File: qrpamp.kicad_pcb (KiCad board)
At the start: 2 copper layers, 101 parts, among them K1 BAND3_IN, K2 BAND2_IN, K3 BAND1_IN, K4 BAND3_OUT, K5 BAND2_OUT, K6 BAND1_OUT, K7 ANT_RLY, P1 PWR, P2 PWR_SW, P3 SWD, P4 ANT, P5 RADIO, P6 PTT_IN, P7 Thumb-Joystick, Q1 MMBT6427, Q2 MMBF170, Q3 IRF510, Q4 IRF510, T1 8:8, T2 8:8, T3 2:3, T4 12:1, T5 1:12, U1 LM7805, U2 LM3940, U3 LCD-2x16, U4 STM32F401xB/C-LQFP

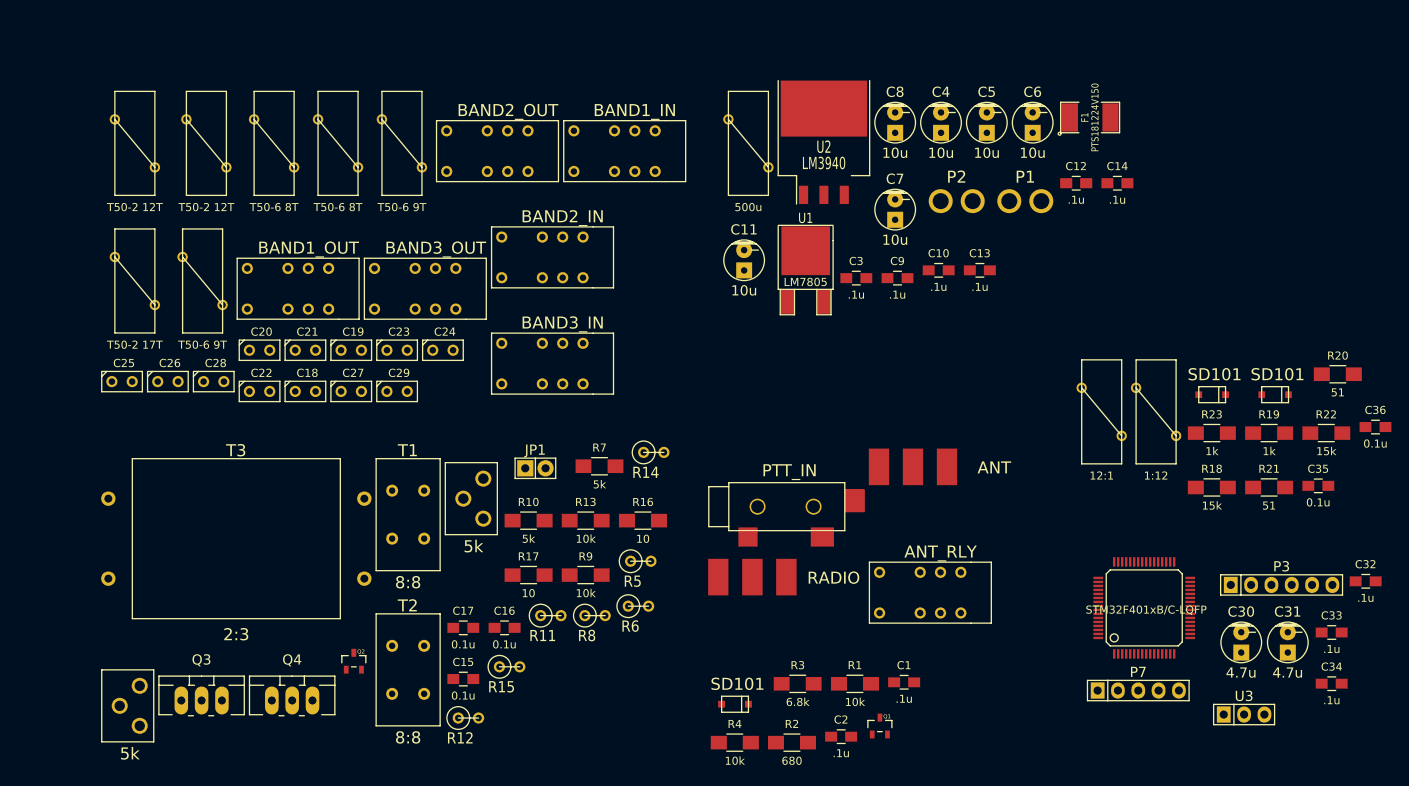
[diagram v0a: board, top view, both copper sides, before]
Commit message: Fixed pin assignment issues in pcb layout
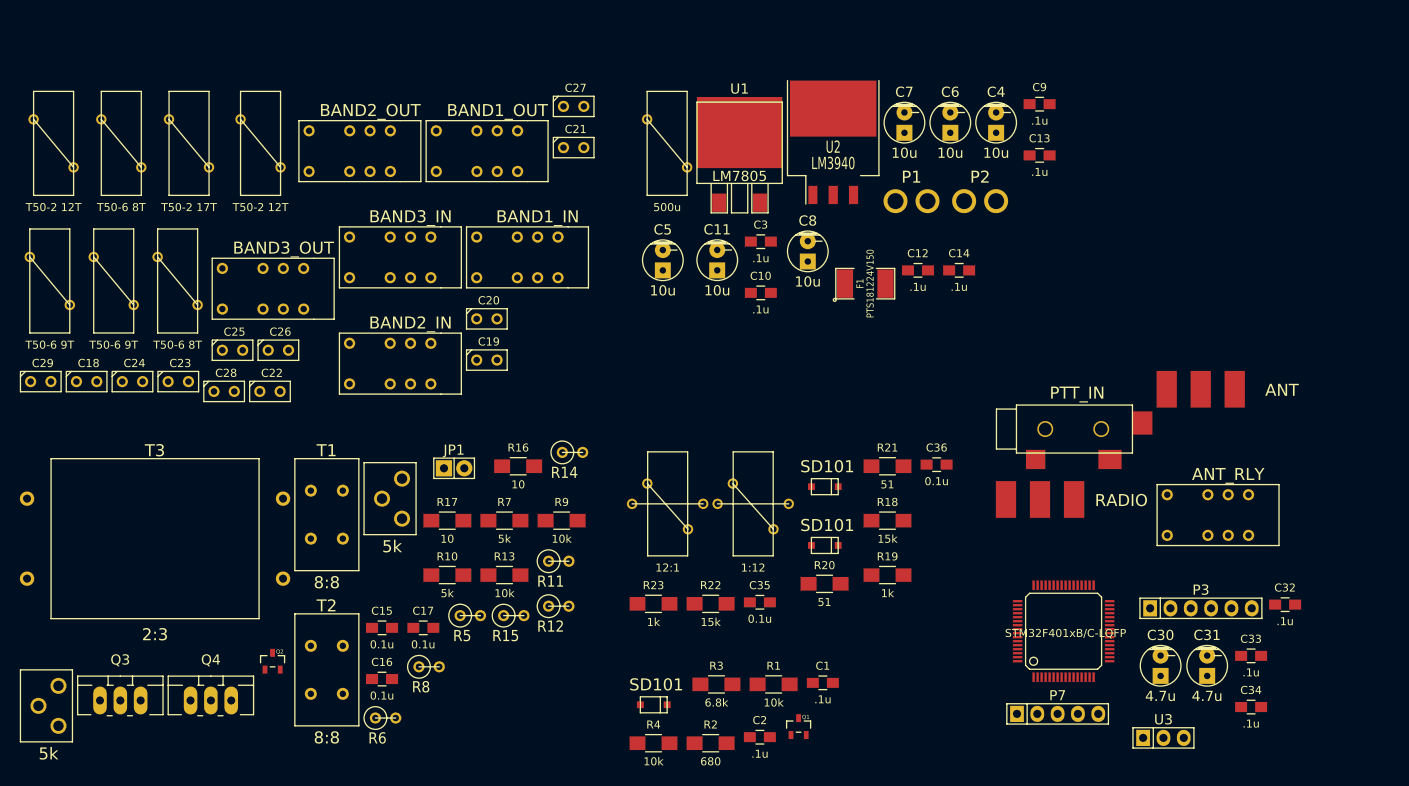
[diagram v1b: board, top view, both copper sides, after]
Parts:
- Q2: footprint Transistors_SMD:sot23 -> nu9j-footprints:sot23-DGS
- T4, T5: footprint nu9j-footprints:TOROID-50 -> nu9j-footprints:TOROID2-50-singleturn
- U1: footprint SMD_Packages:DPAK-2 -> nu9j-footprints:DPAK-3_VIVOGND
- U2: footprint SMD_Packages:TO-263 -> nu9j-footprints:TO-263_VIVOGND
- moved R22 79.9 mm to (155.2, 119.1)
- moved R23 73.0 mm to (148.0, 119.1)
- moved C35 71.3 mm to (161.3, 118.9)
- moved R20 69.3 mm to (169.4, 116.6)
- moved D5 57.5 mm to (167.8, 104.4)
- moved T4 55.5 mm to (149.8, 106.6)
- moved C36 55.1 mm to (183.4, 101.7)
- moved D4 52.0 mm to (167.8, 111.8)
- moved T5 51.7 mm to (160.5, 106.6)
- moved R19 50.9 mm to (177.3, 115.5)
- moved R21 47.8 mm to (177.3, 101.9)
- moved C27 45.2 mm to (138.1, 56.9)
- moved C29 44.6 mm to (71.4, 91.3)
- moved C5 44.0 mm to (149.2, 76.1)
- moved C21 42.0 mm to (138.1, 62.0)
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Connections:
- K1 pad 1: Net-(K1-Pad1) -> +12V
- K1 pad 10: (no net) -> Net-(K1-Pad10)
- K1 pad 12: /Amplifier/amp_out -> /Band Filters/bandfilter_3sel
- K1 pad 3: Net-(K1-Pad14) -> Net-(K1-Pad10)
- K1 pad 4: (no net) -> /Amplifier/amp_out
- K1 pad 5: /Amplifier/amp_out -> Net-(K1-Pad5)
- K1 pad 8: +12V -> Net-(K1-Pad5)
- K1 pad 9: /Band Filters/bandfilter_3sel -> /Amplifier/amp_out
- K2 pad 1: Net-(C19-Pad1) -> +12V
- K2 pad 10: (no net) -> Net-(K2-Pad10)
- K2 pad 12: Net-(K1-Pad14) -> /Band Filters/bandfilter_2sel
- K2 pad 3: Net-(K2-Pad14) -> Net-(K2-Pad10)
- K2 pad 4: (no net) -> Net-(K1-Pad10)
- K2 pad 5: Net-(K1-Pad14) -> Net-(C19-Pad1)
- K2 pad 8: +12V -> Net-(C19-Pad1)
- K2 pad 9: /Band Filters/bandfilter_2sel -> Net-(K1-Pad10)
- K3 pad 1: Net-(C20-Pad1) -> +12V
- K3 pad 10: (no net) -> Net-(C21-Pad1)
- K3 pad 12: Net-(K2-Pad14) -> /Band Filters/bandfilter_1sel
- K3 pad 4: (no net) -> Net-(K2-Pad10)
- K3 pad 5: Net-(K2-Pad14) -> Net-(C20-Pad1)
- K3 pad 8: +12V -> Net-(C20-Pad1)
- K3 pad 9: /Band Filters/bandfilter_1sel -> Net-(K2-Pad10)
- K4 pad 1: Net-(C26-Pad1) -> +12V
- K4 pad 10: (no net) -> Net-(K4-Pad10)
- K4 pad 12: /Band Filters/bandfilter_out -> /Band Filters/bandfilter_3sel
- K4 pad 3: Net-(K4-Pad14) -> Net-(K4-Pad10)
- K4 pad 4: (no net) -> /Band Filters/bandfilter_out
- K4 pad 5: /Band Filters/bandfilter_out -> Net-(C26-Pad1)
- K4 pad 8: +12V -> Net-(C26-Pad1)
- K4 pad 9: /Band Filters/bandfilter_3sel -> /Band Filters/bandfilter_out
- K5 pad 1: Net-(C27-Pad1) -> +12V
- K5 pad 10: (no net) -> Net-(K5-Pad10)
- K5 pad 12: Net-(K4-Pad14) -> /Band Filters/bandfilter_2sel
- K5 pad 3: Net-(K5-Pad14) -> Net-(K5-Pad10)
- K5 pad 4: (no net) -> Net-(K4-Pad10)
- K5 pad 5: Net-(K4-Pad14) -> Net-(C27-Pad1)
- K5 pad 8: +12V -> Net-(C27-Pad1)
- K5 pad 9: /Band Filters/bandfilter_2sel -> Net-(K4-Pad10)
- K6 pad 1: Net-(C28-Pad1) -> +12V
- K6 pad 10: (no net) -> Net-(C25-Pad1)
- K6 pad 12: Net-(K5-Pad14) -> /Band Filters/bandfilter_1sel
- K6 pad 4: (no net) -> Net-(K5-Pad10)
- K6 pad 5: Net-(K5-Pad14) -> Net-(C28-Pad1)
- K6 pad 8: +12V -> Net-(C28-Pad1)
- K6 pad 9: /Band Filters/bandfilter_1sel -> Net-(K5-Pad10)
- K7 pad 1: /Amplifier/amp_in -> +12V
- K7 pad 10: (no net) -> Net-(K7-Pad10)
- K7 pad 12: Net-(K7-Pad12) -> /RF In/Out/ant_sw_rly
- K7 pad 3: Net-(K7-Pad14) -> Net-(K7-Pad10)
- K7 pad 4: (no net) -> Net-(K7-Pad4)
- K7 pad 5: /RF In/Out/raw_input -> /RF In/Out/from_final
- K7 pad 8: +12V -> /Amplifier/amp_in
- K7 pad 9: /RF In/Out/ant_sw_rly -> /RF In/Out/raw_input
- L2 pad 1: Net-(K1-Pad1) -> Net-(K1-Pad5)
- P4 pad 1: Net-(K7-Pad12) -> Net-(K7-Pad4)
- T5 pad 1: /Band Filters/bandfilter_out -> Net-(D5-Pad1)
- T5 pad 2: GND -> Net-(D4-Pad1)

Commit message: Separate analog/digital gnd. Add some filtering caps and reset button.
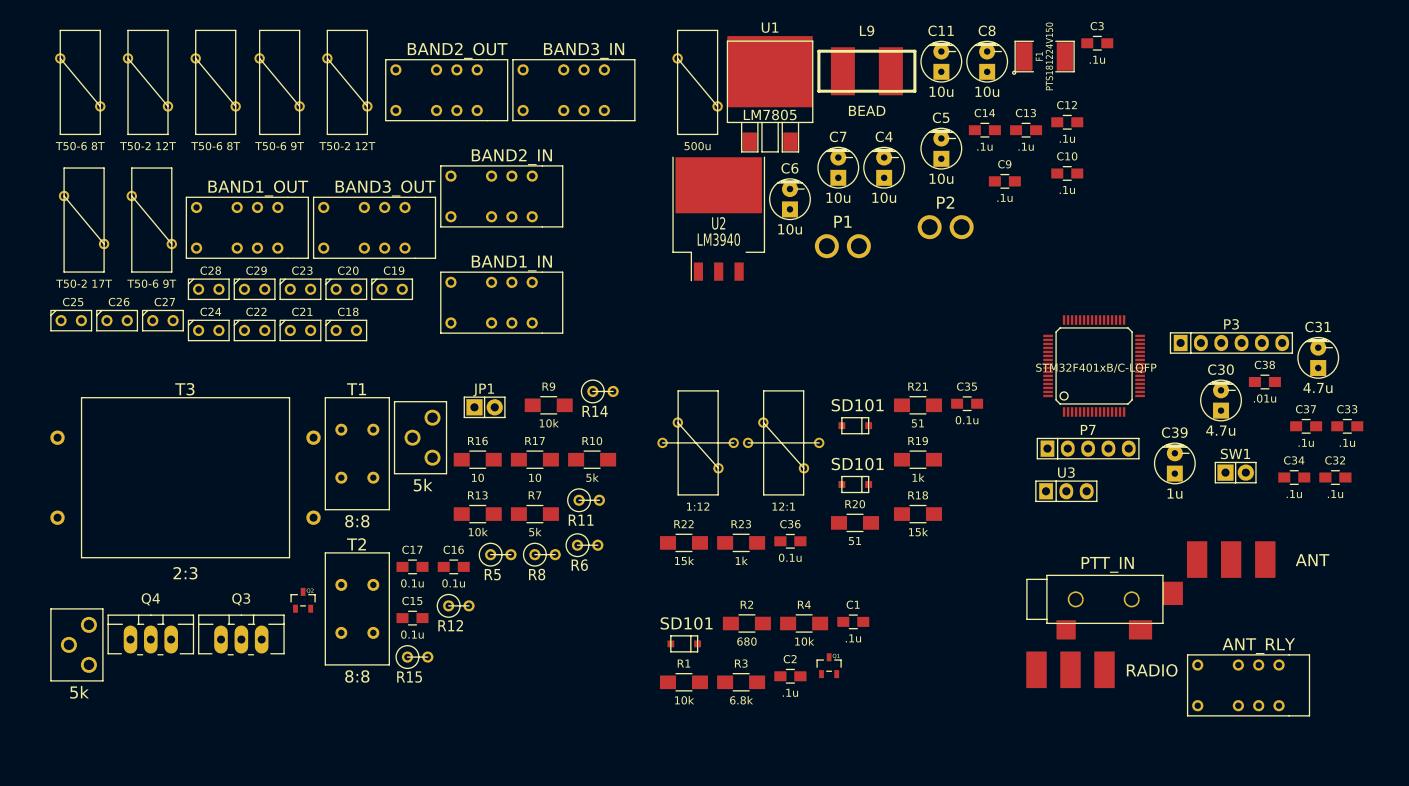
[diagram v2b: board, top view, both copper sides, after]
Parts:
- added C37: .1u, Capacitors_SMD:C_0805_HandSoldering, F.Cu at (229.6, 96.9)
- added C38: .01u, Capacitors_SMD:C_0805_HandSoldering, F.Cu at (224.5, 91.3)
- added C39: 1u, Capacitors_ThroughHole:Capacitor5x11RM2.5, F.Cu at (213.2, 101.5)
- added L9: BEAD, nu9j-footprints:WE-SUCKW, F.Cu at (174.7, 52.5)
- added SW1: SW_PUSH, Pin_Headers:Pin_Header_Straight_1x02, F.Cu at (220.8, 102.7)
- moved C27 57.9 mm to (86.7, 83.7)
- moved C3 48.8 mm to (203.5, 49.0)
- moved C10 41.1 mm to (199.8, 65.3)
- moved C21 41.1 mm to (103.9, 84.9)
- moved C31 40.9 mm to (231.1, 88.3)
- moved C5 37.5 mm to (184.0, 62.2)
- moved C11 37.4 mm to (184.0, 51.3)
- moved F1 36.2 mm to (196.9, 50.7)
- moved C35 35.9 mm to (187.2, 94.1)
- moved C30 34.0 mm to (219.0, 93.7)
- moved P3 33.4 mm to (220.3, 86.5)
- moved P7 33.4 mm to (202.4, 99.7)
- moved U4 33.4 mm to (199.4, 95.1)
- moved R6 33.2 mm to (139.8, 111.7)
- moved U3 33.1 mm to (199.6, 105.0)
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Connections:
- C30 pad 2: GND -> DGND
- C31 pad 2: GND -> DGND
- C32 pad 2: GND -> DGND
- C33 pad 2: GND -> DGND
- C34 pad 2: GND -> DGND
- K1 pad 1: +12V -> Net-(K1-Pad1)
- K1 pad 10: Net-(K1-Pad10) -> (no net)
- K1 pad 12: /Band Filters/bandfilter_3sel -> /Amplifier/amp_out
- K1 pad 3: Net-(K1-Pad10) -> Net-(K1-Pad14)
- K1 pad 4: /Amplifier/amp_out -> (no net)
- K1 pad 5: Net-(K1-Pad5) -> /Amplifier/amp_out
- K1 pad 8: Net-(K1-Pad5) -> +12V
- K1 pad 9: /Amplifier/amp_out -> /Band Filters/bandfilter_3sel
- K2 pad 1: +12V -> Net-(C19-Pad1)
- K2 pad 10: Net-(K2-Pad10) -> (no net)
- K2 pad 12: /Band Filters/bandfilter_2sel -> Net-(K1-Pad14)
- K2 pad 3: Net-(K2-Pad10) -> Net-(K2-Pad14)
- K2 pad 4: Net-(K1-Pad10) -> (no net)
- K2 pad 5: Net-(C19-Pad1) -> Net-(K1-Pad14)
- K2 pad 8: Net-(C19-Pad1) -> +12V
- K2 pad 9: Net-(K1-Pad10) -> /Band Filters/bandfilter_2sel
- K3 pad 1: +12V -> Net-(C20-Pad1)
- K3 pad 10: Net-(C21-Pad1) -> (no net)
- K3 pad 12: /Band Filters/bandfilter_1sel -> Net-(K2-Pad14)
- K3 pad 4: Net-(K2-Pad10) -> (no net)
- K3 pad 5: Net-(C20-Pad1) -> Net-(K2-Pad14)
- K3 pad 8: Net-(C20-Pad1) -> +12V
- K3 pad 9: Net-(K2-Pad10) -> /Band Filters/bandfilter_1sel
- K4 pad 1: +12V -> Net-(C26-Pad1)
- K4 pad 10: Net-(K4-Pad10) -> (no net)
- K4 pad 12: /Band Filters/bandfilter_3sel -> /Band Filters/bandfilter_out
- K4 pad 3: Net-(K4-Pad10) -> Net-(K4-Pad14)
- K4 pad 4: /Band Filters/bandfilter_out -> (no net)
- K4 pad 5: Net-(C26-Pad1) -> /Band Filters/bandfilter_out
- K4 pad 8: Net-(C26-Pad1) -> +12V
- K4 pad 9: /Band Filters/bandfilter_out -> /Band Filters/bandfilter_3sel
- K5 pad 1: +12V -> Net-(C27-Pad1)
- K5 pad 10: Net-(K5-Pad10) -> (no net)
- K5 pad 12: /Band Filters/bandfilter_2sel -> Net-(K4-Pad14)
- K5 pad 3: Net-(K5-Pad10) -> Net-(K5-Pad14)
- K5 pad 4: Net-(K4-Pad10) -> (no net)
- K5 pad 5: Net-(C27-Pad1) -> Net-(K4-Pad14)
- K5 pad 8: Net-(C27-Pad1) -> +12V
- K5 pad 9: Net-(K4-Pad10) -> /Band Filters/bandfilter_2sel
- K6 pad 1: +12V -> Net-(C28-Pad1)
- K6 pad 10: Net-(C25-Pad1) -> (no net)
- K6 pad 12: /Band Filters/bandfilter_1sel -> Net-(K5-Pad14)
- K6 pad 4: Net-(K5-Pad10) -> (no net)
- K6 pad 5: Net-(C28-Pad1) -> Net-(K5-Pad14)
- K6 pad 8: Net-(C28-Pad1) -> +12V
- K6 pad 9: Net-(K5-Pad10) -> /Band Filters/bandfilter_1sel
- K7 pad 1: +12V -> /Amplifier/amp_in
- K7 pad 10: Net-(K7-Pad10) -> (no net)
- K7 pad 12: /RF In/Out/ant_sw_rly -> Net-(K7-Pad12)
- K7 pad 3: Net-(K7-Pad10) -> Net-(K7-Pad14)
- K7 pad 4: Net-(K7-Pad4) -> (no net)
- K7 pad 5: /RF In/Out/from_final -> /RF In/Out/raw_input
- K7 pad 8: /Amplifier/amp_in -> +12V
- K7 pad 9: /RF In/Out/raw_input -> /RF In/Out/ant_sw_rly
- L2 pad 1: Net-(K1-Pad5) -> Net-(K1-Pad1)
- P3 pad 3: GND -> DGND
- P4 pad 1: Net-(K7-Pad4) -> Net-(K7-Pad12)
- P7 pad 5: GND -> DGND
- U3 pad 2: GND -> DGND
- U4 pad 12: Net-(U4-Pad12) -> DGND
- U4 pad 13: Net-(U4-Pad13) -> +3.3V
- U4 pad 18: GND -> DGND
